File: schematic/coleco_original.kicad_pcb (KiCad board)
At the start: 2 copper layers, 88.7 x 114.3 mm, 62 parts, among them J1 Barrel_Jack_Switch, J2 Conn_01x02, J3 Conn_Coaxial, J4 Cartridge Port, J5 Player 1, J6 Conn_02x05_Odd_Even, J7 Player 2, J8 Conn_01x03, Q1 2N3904, SW1 SW_Push, U1 LM386, U2 SN76489AN, U3 Z84C0010AEG, U4 6116XA, U5 AT27C256R-70JU-T, U6 TMS9118NL, U7 TMS4416, U8 TMS4416, U9 EPM7064SLC, Y1 Crystal

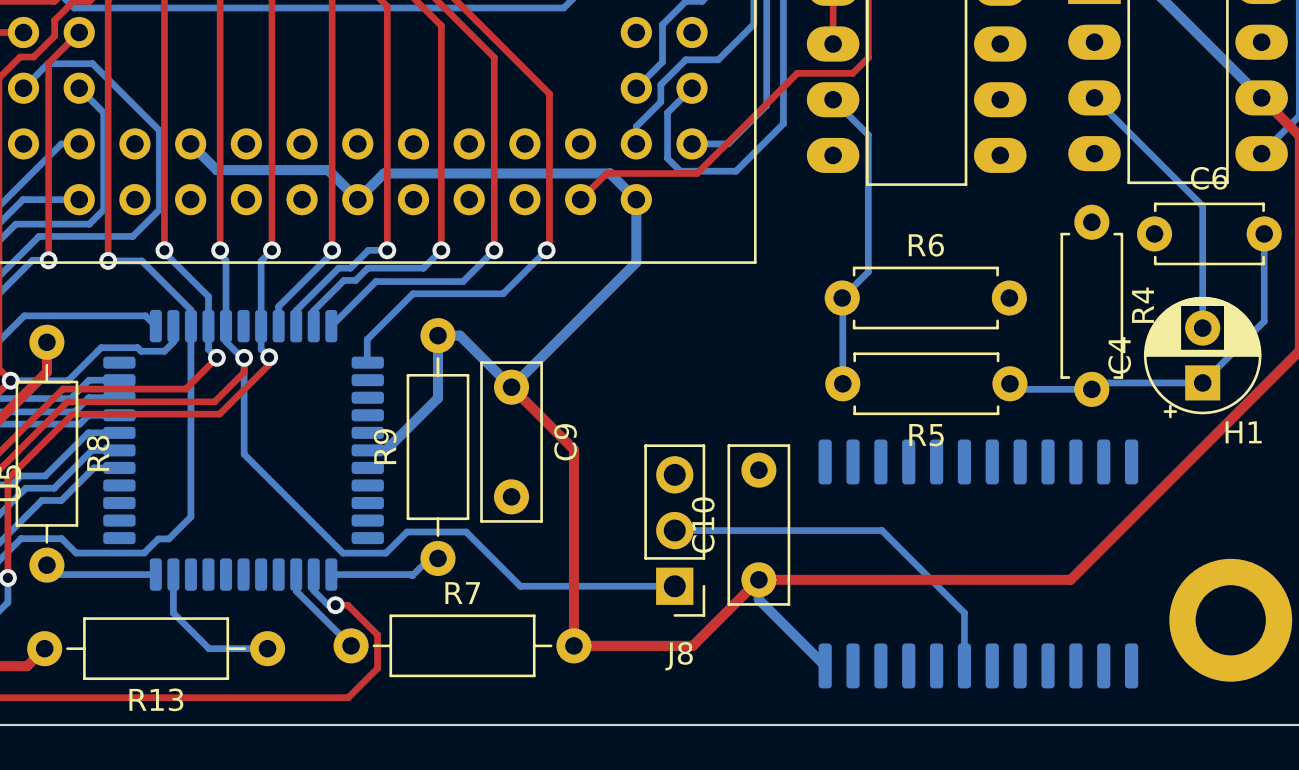
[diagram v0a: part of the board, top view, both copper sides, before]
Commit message: added some data lines to pcb
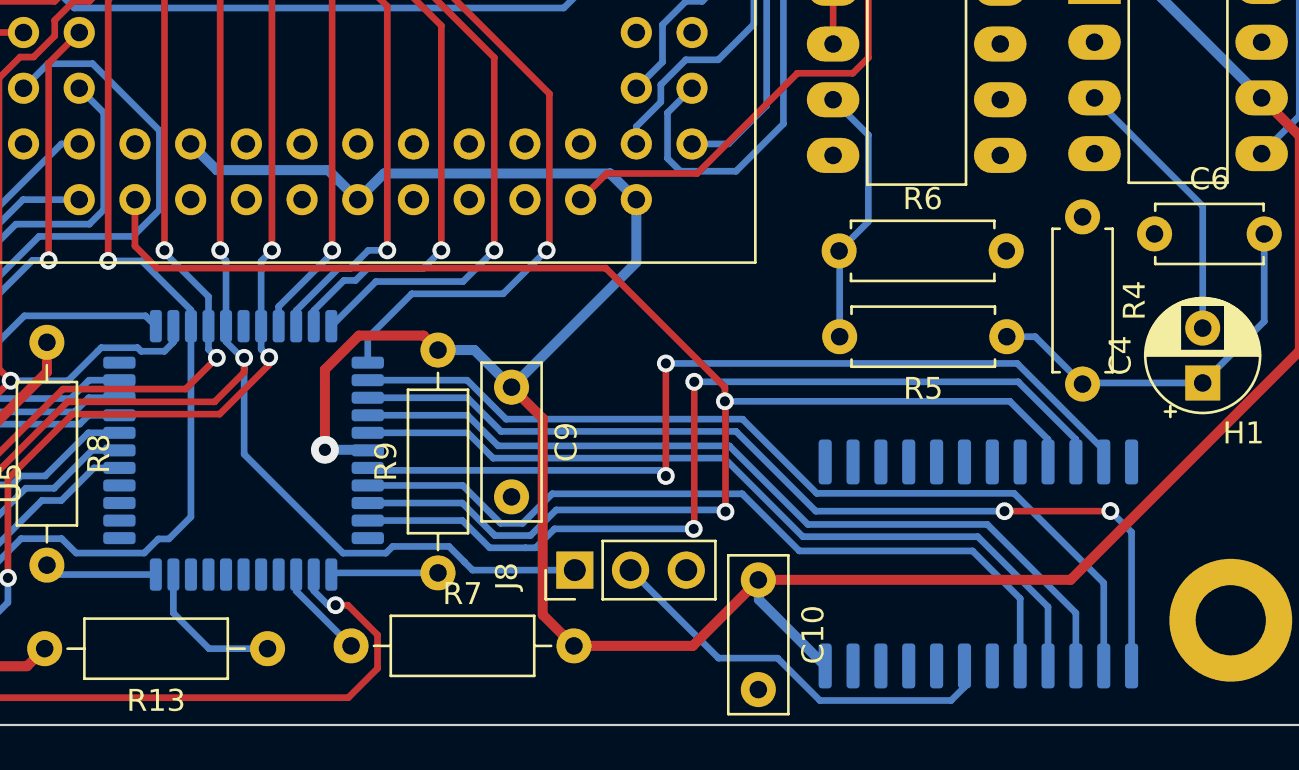
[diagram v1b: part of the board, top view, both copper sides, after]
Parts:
- moved J8 4.62 mm to (136.8, 162.6), turned to 90 degrees
- moved R5 2.15 mm to (156.5, 152.0)
- moved R6 2.15 mm to (148.9, 148.1)
- moved R9 0.66 mm to (130.6, 162.8)
- moved R4 0.49 mm to (160.0, 146.5)
- turned C10 to -90 degrees
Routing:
- net /GLUE/D0: track 49.0 -> 120.2 mm, vias 0 -> 2
- net /GLUE/D3: track 55.7 -> 99.2 mm, vias 0 -> 2
- net /GLUE/D1: track 54.9 -> 96.9 mm, vias 0 -> 2
- net /GLUE/D4: track 63.5 -> 104.6 mm
- net /GLUE/D2: track 54.9 -> 95.9 mm, vias 0 -> 2
- net /GLUE/D5: track 57.5 -> 95.9 mm
- net /GLUE/D6: track 62.2 -> 99.2 mm
- net /GLUE/D7: track 55.3 -> 91.4 mm
- net /GLUE/A10: track 93.7 -> 88.3 mm
- net +5V: track 544.6 -> 549.0 mm, vias 0 -> 1
- net Net-(U2-OUT): track 14.1 -> 12.0 mm
- net Net-(J8-Pin_2): track 17.2 -> 18.9 mm
- net Net-(C4-Pad1): track 17.0 -> 17.8 mm

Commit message: first prototype board complete with smd ram
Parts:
- C9: footprint Capacitor_THT:C_Disc_D7.0mm_W2.5mm_P5.00mm -> Capacitor_SMD:C_1206_3216Metric; moved to B.Cu
- R13, R7, R8, R9: footprint Resistor_THT:R_Axial_DIN0207_L6.3mm_D2.5mm_P10.16mm_Horizontal -> Resistor_SMD:R_0805_2012Metric; moved to B.Cu
- moved C9 32.0 mm to (135.5, 122.3)
- moved U3 27.4 mm to (128.2, 130.6)
- moved R7 27.4 mm to (130.7, 139.1), turned to -90 degrees
- moved R9 23.9 mm to (132.8, 139.0), turned to -90 degrees
- moved U4 21.9 mm to (133.9, 157.6), turned to 0 degrees
- moved R13 17.8 mm to (121.9, 148.4), turned to -90 degrees
- moved R8 17.6 mm to (122.5, 137.6), turned to 90 degrees
- moved J2 15.7 mm to (165.6, 106.2)
- moved C11 14.4 mm to (101.1, 155.4)
- moved J8 8.72 mm to (145.6, 162.8), turned to 180 degrees
- moved SW1 5.78 mm to (93.4, 148.1), turned to 90 degrees
- moved U5 5.40 mm to (109.9, 157.9), turned to 90 degrees
- moved C1 3.87 mm to (94.2, 135.0)
- moved C10 3.61 mm to (141.9, 164.6), turned to 90 degrees
- moved R2 3.43 mm to (91.2, 131.7)
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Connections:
- H5 pad 1: GND -> GNDD
- U9 pad 35: /GLUE/D0 -> /GLUE/~{M1}
- U9 pad 36: /GLUE/D1 -> /GLUE/~{RFSH}
- U9 pad 37: /GLUE/D2 -> /GLUE/~{RESET}
- U9 pad 39: /GLUE/D3 -> /GLUE/~{WAIT}
- U9 pad 40: /GLUE/D4 -> /GLUE/~{BUSRQ}
- U9 pad 41: /GLUE/D5 -> /GLUE/~{BUSAK}
- U9 pad 44: /GLUE/D6 -> /GLUE/~{IORQ}
- U9 pad 45: /GLUE/D7 -> /GLUE/~{MREQ}
- U9 pad 46: /GLUE/~{M1} -> /GLUE/D0
- U9 pad 48: /GLUE/~{RFSH} -> /GLUE/D1
- U9 pad 49: /GLUE/~{IORQ} -> /GLUE/D7
- U9 pad 50: /GLUE/~{MREQ} -> /GLUE/D2
- U9 pad 51: /GLUE/~{WAIT} -> /GLUE/D6
- U9 pad 52: /GLUE/~{RESET} -> /GLUE/D5
- U9 pad 54: /GLUE/~{CS_h8000} -> /GLUE/D4
- U9 pad 55: /GLUE/~{CS_hA000} -> /GLUE/D3
- U9 pad 56: /GLUE/~{CS_hC000} -> /GLUE/~{ROM_ENABLE}
- U9 pad 57: /GLUE/~{CS_hE000} -> /GLUE/~{RAM_CS}
- U9 pad 58: /GLUE/~{ROM_ENABLE} -> /GLUE/~{SND_ENABLE}
- U9 pad 60: /GLUE/~{RAM_CS} -> /GLUE/RX
- U9 pad 61: /GLUE/~{CSW} -> /GLUE/TX
- U9 pad 63: /GLUE/~{CSR} -> /GLUE/~{CS_hC000}
- U9 pad 64: /GLUE/~{SND_ENABLE} -> /GLUE/~{CS_hA000}
- U9 pad 65: /GLUE/C2P0 -> /GLUE/~{CS_h8000}
- U9 pad 67: /GLUE/C2P1 -> /GLUE/~{CS_hE000}
- U9 pad 68: /GLUE/C2P2 -> /GLUE/~{CSR}
- U9 pad 69: /GLUE/C2P3 -> /GLUE/~{CSW}
- U9 pad 70: /GLUE/C2P4 -> /GLUE/C2P0
- U9 pad 73: /GLUE/C2P5 -> /GLUE/C2P1
- U9 pad 74: /GLUE/C2P6 -> /GLUE/C2P2
- U9 pad 75: /GLUE/C2P7 -> /GLUE/C2P3
- U9 pad 76: /GLUE/C2P8 -> /GLUE/C2P4
- U9 pad 77: /GLUE/~{BUSRQ} -> /GLUE/C2P5
- U9 pad 79: /GLUE/~{BUSAK} -> /GLUE/C2P6
- U9 pad 80: /GLUE/RX -> /GLUE/C2P7
- U9 pad 81: /GLUE/TX -> /GLUE/C2P8
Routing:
- net /GLUE/A10: track 88.3 -> 220.3 mm, vias 3 -> 1
- net /GLUE/D7: track 91.4 -> 221.8 mm, vias 0 -> 1
- net /GLUE/D6: track 99.2 -> 221.1 mm, vias 0 -> 1
- net /GLUE/~{RESET}: track 0.00 -> 101.8 mm, vias 0 -> 3
- net /GLUE/D5: track 95.9 -> 190.3 mm, vias 0 -> 1
- net /GLUE/D4: track 104.6 -> 198.4 mm, vias 0 -> 1
- net /GLUE/D2: track 95.9 -> 187.8 mm
- net /GLUE/A8: track 85.4 -> 176.9 mm
- net /GLUE/D1: track 96.9 -> 180.2 mm
- net /GLUE/A9: track 90.7 -> 172.0 mm, vias 3 -> 2
- net /GLUE/D3: track 99.2 -> 177.4 mm
- net /GLUE/C1P0: track 0.00 -> 76.4 mm, vias 0 -> 1
- net /GLUE/C1P1: track 0.00 -> 71.8 mm, vias 0 -> 1
- net /GLUE/C1P5: track 0.00 -> 68.5 mm
- net /GLUE/C1P6: track 0.00 -> 66.6 mm
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- added copper zone on B.Cu, net GNDD
- added copper zone on F.Cu, net GNDD
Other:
- board size 88.7 x 114.3 mm -> 88.7 x 118.1 mm

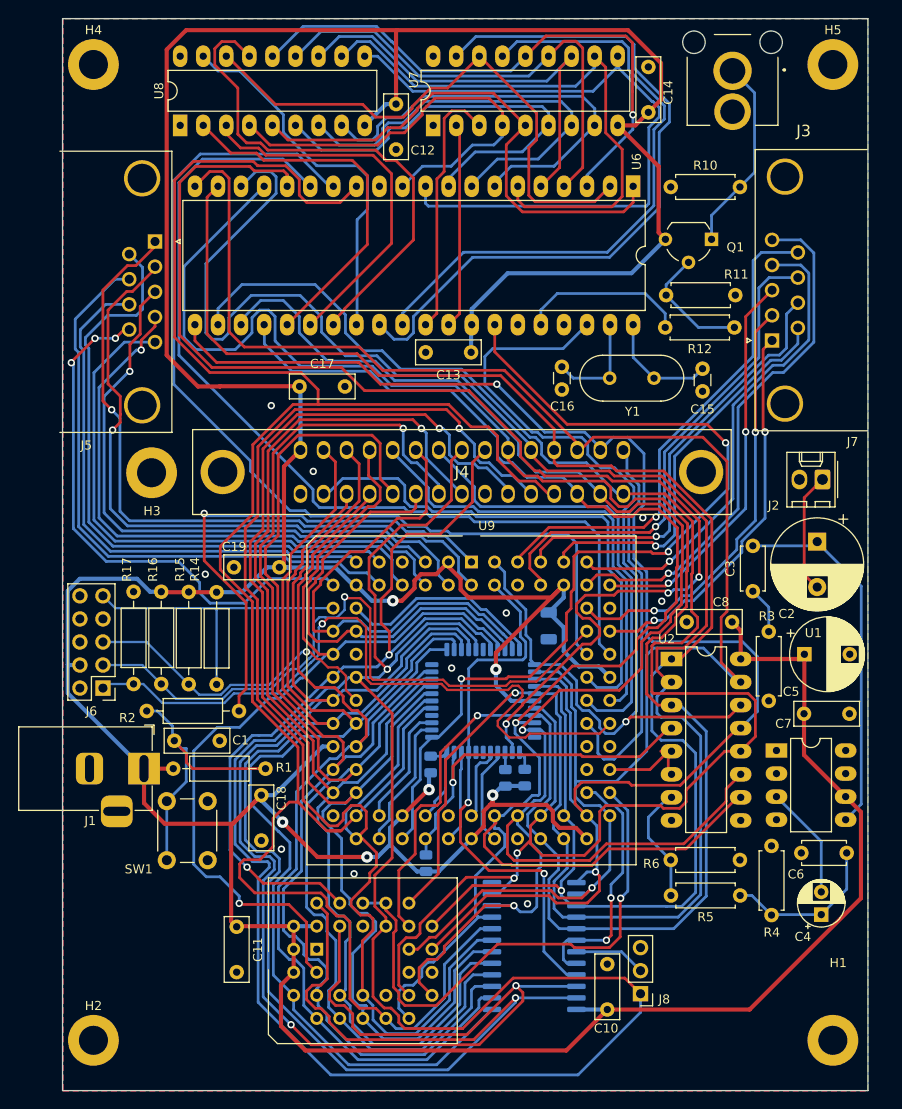
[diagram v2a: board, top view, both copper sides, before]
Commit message: First version sent out for build. 6116 as a DIP makes the design easier.
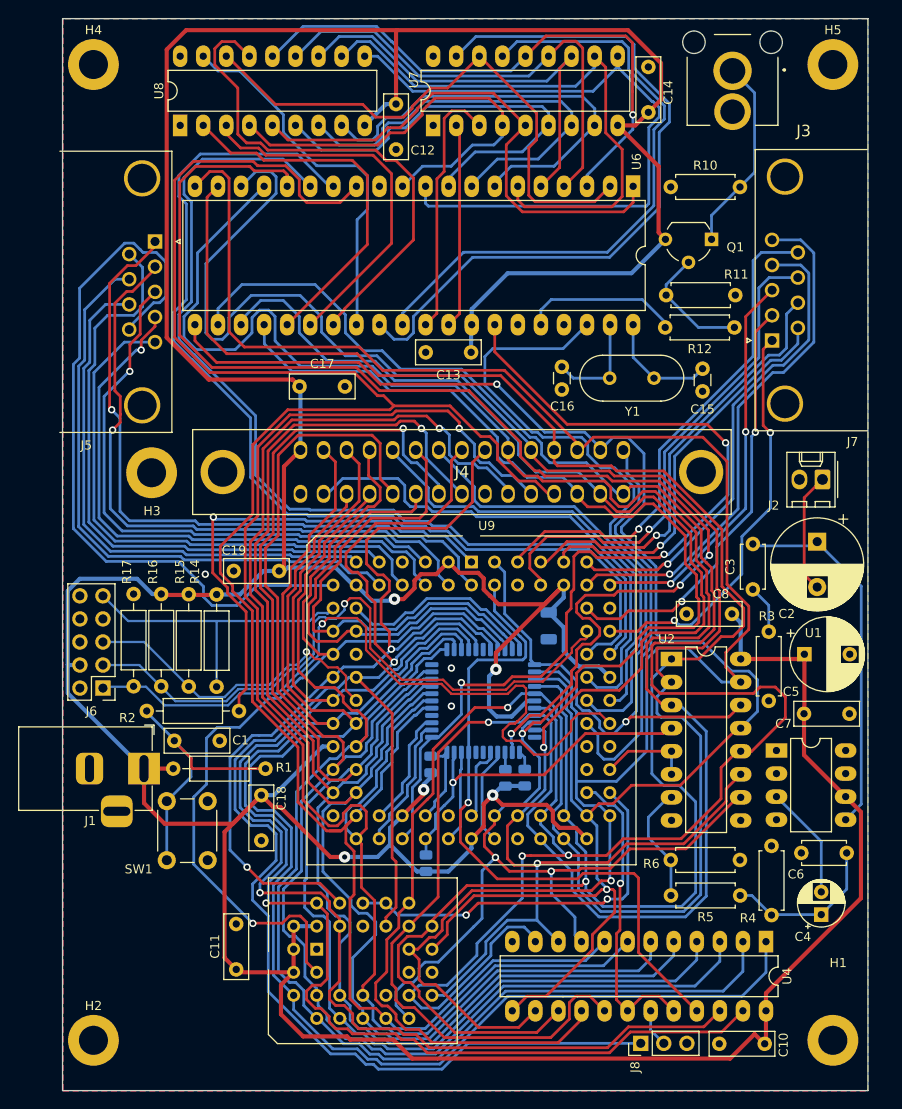
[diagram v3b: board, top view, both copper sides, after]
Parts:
- U4: footprint Package_SO:SOIC-24W_7.5x15.4mm_P1.27mm -> Package_DIP:DIP-24_W7.62mm_LongPads; moved to F.Cu
- moved U4 25.5 mm to (159.4, 157.1), turned to -90 degrees
- moved C10 17.7 mm to (159.2, 168.3), turned to 180 degrees
- moved J8 5.46 mm to (145.6, 168.3), turned to 90 degrees
- moved C11 4.70 mm to (101.0, 160.1), turned to 90 degrees
- moved C8 0.89 mm to (155.6, 121.0)
- moved C19 0.41 mm to (105.8, 116.3)
- moved R16 0.25 mm to (92.8, 129.0)
- moved R17 0.25 mm to (89.7, 129.0)
- moved R14 0.25 mm to (98.9, 129.0)
- moved R15 0.25 mm to (95.8, 129.0)
- moved C3 0.20 mm to (157.9, 118.3)
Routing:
- net /GLUE/A10: track 220.3 -> 175.0 mm
- net /GLUE/D6: track 221.1 -> 258.6 mm
- net /GLUE/A7: track 120.2 -> 156.3 mm
- net /GLUE/D7: track 221.8 -> 256.7 mm
- net /GLUE/D5: track 190.3 -> 224.1 mm
- net /GLUE/A6: track 113.2 -> 144.9 mm
- net /GLUE/A5: track 133.4 -> 159.2 mm
- net /GLUE/A4: track 138.6 -> 162.0 mm
- net /GLUE/D2: track 187.8 -> 210.7 mm
- net /GLUE/C1P8: track 60.4 -> 82.7 mm, vias 3 -> 0
- net /GLUE/A3: track 138.3 -> 158.3 mm
- net /GLUE/D4: track 198.4 -> 217.9 mm
- net /GLUE/A8: track 176.9 -> 157.9 mm
- net /GLUE/A9: track 172.0 -> 153.2 mm, vias 2 -> 1
- net /GLUE/~{ROM_ENABLE}: track 59.1 -> 42.6 mm, vias 1 -> 2
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
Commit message: changed traces to 8 mil, 8 mil iso. allows for better routing of lines that didn't need to be as thick as they were.
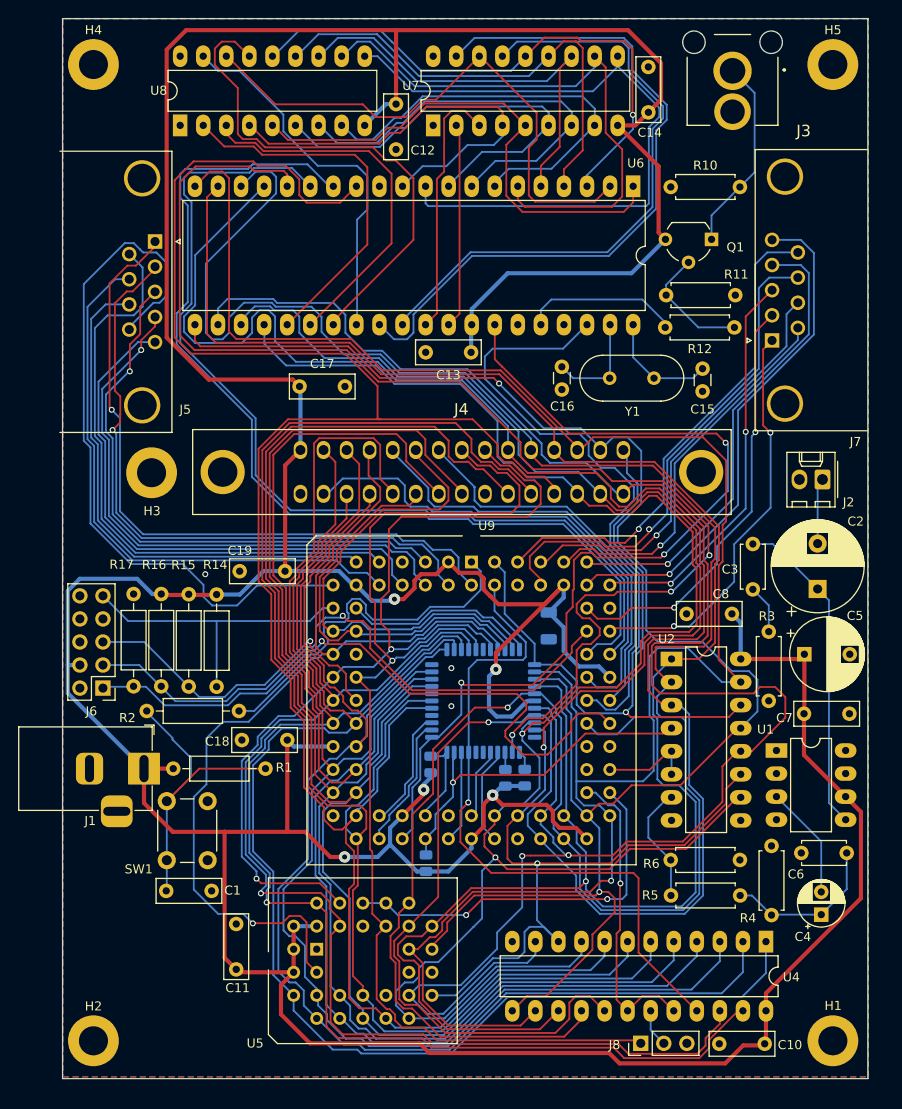
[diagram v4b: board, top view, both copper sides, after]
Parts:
- moved C1 16.6 mm to (93.3, 151.5)
- moved C18 6.71 mm to (106.7, 134.9), turned to 180 degrees
- moved C2 5.21 mm to (165.1, 118.2), turned to 90 degrees
- moved C19 0.66 mm to (106.4, 116.3)
- moved H1 0.05 mm to (166.8, 168.0)
- moved H2 0.05 mm to (85.3, 168.0)
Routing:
- net /GLUE/A10: track 175.0 -> 129.0 mm
- net /GLUE/D0: track 181.3 -> 197.1 mm, vias 3 -> 2
- net /GLUE/~{RESET_SW}: track 53.7 -> 41.0 mm, vias 1 -> 0
- net /GLUE/TCK: track 81.0 -> 73.4 mm
- net /GLUE/A8: track 157.9 -> 151.2 mm
- net /GLUE/A5: track 159.2 -> 153.1 mm
- net /GLUE/A1: track 167.5 -> 161.6 mm, vias 1 -> 0
- net /GLUE/A11: track 95.5 -> 101.2 mm
- net /GLUE/~{CS_hC000}: track 44.5 -> 38.8 mm
- net /GLUE/A2: track 165.5 -> 159.9 mm, vias 1 -> 0
- net /GLUE/A7: track 156.3 -> 150.8 mm
- net Net-(J2-Pin_1): track 13.3 -> 7.93 mm
- net /GLUE/A4: track 162.0 -> 157.3 mm, vias 1 -> 0
- net /GLUE/TDO: track 72.3 -> 67.7 mm
- net Net-(C2-Pad1): track 40.6 -> 36.2 mm
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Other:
- board size 88.7 x 118.1 mm -> 88.7 x 116.7 mm

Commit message: first ok version of no intn dev board.
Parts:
- moved C9 6.79 mm to (136.1, 129.1), turned to 90 degrees
- moved R8 1.59 mm to (121.8, 139.0)
- moved C11 1.53 mm to (102.6, 160.3)
- moved R3 1.05 mm to (160.2, 131.5)
- moved U3 0.89 mm to (127.4, 130.6)
- moved R5 0.84 mm to (156.5, 151.2)
- moved C8 0.19 mm to (155.8, 121.0)
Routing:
- net /GLUE/~{WAIT}: track 38.8 -> 91.1 mm, vias 1 -> 0
- net /GLUE/TMS: track 37.0 -> 60.4 mm, vias 1 -> 0
- net /GLUE/D7: track 254.1 -> 234.6 mm
- net /GLUE/TDO: track 67.7 -> 85.6 mm, vias 1 -> 0
- net /GLUE/CLK: track 105.5 -> 92.2 mm
- net /GLUE/D3: track 190.6 -> 200.9 mm
- net /GLUE/A12: track 104.3 -> 94.1 mm, vias 1 -> 0
- net /GLUE/D6: track 254.4 -> 245.2 mm, vias 1 -> 2
- net /GLUE/A10: track 129.0 -> 134.9 mm
- net /cpu/~{NMI}: track 142.5 -> 147.4 mm, vias 3 -> 1
- net /GLUE/D4: track 219.1 -> 215.6 mm
- net /GLUE/D2: track 209.6 -> 206.2 mm, vias 2 -> 1
- net /GLUE/TCK: track 73.4 -> 70.2 mm
- net /GLUE/A0: track 230.0 -> 226.9 mm
- net /GLUE/~{WR}: track 74.2 -> 71.7 mm
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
